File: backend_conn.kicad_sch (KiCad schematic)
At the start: 1 part, among them J2 QSH-030-01-X-D-A-XX

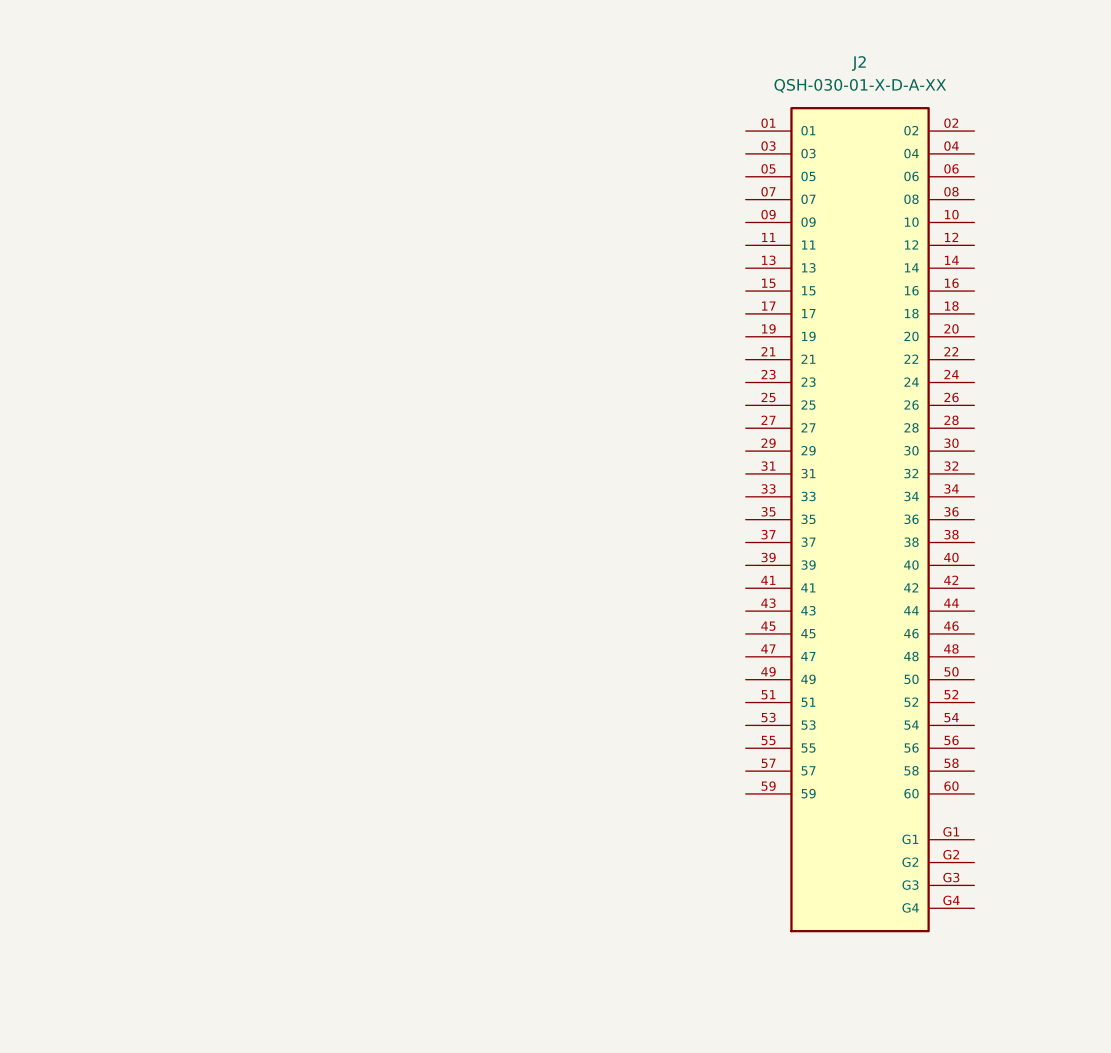
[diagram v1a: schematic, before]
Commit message: started changing package, added correct decoupling
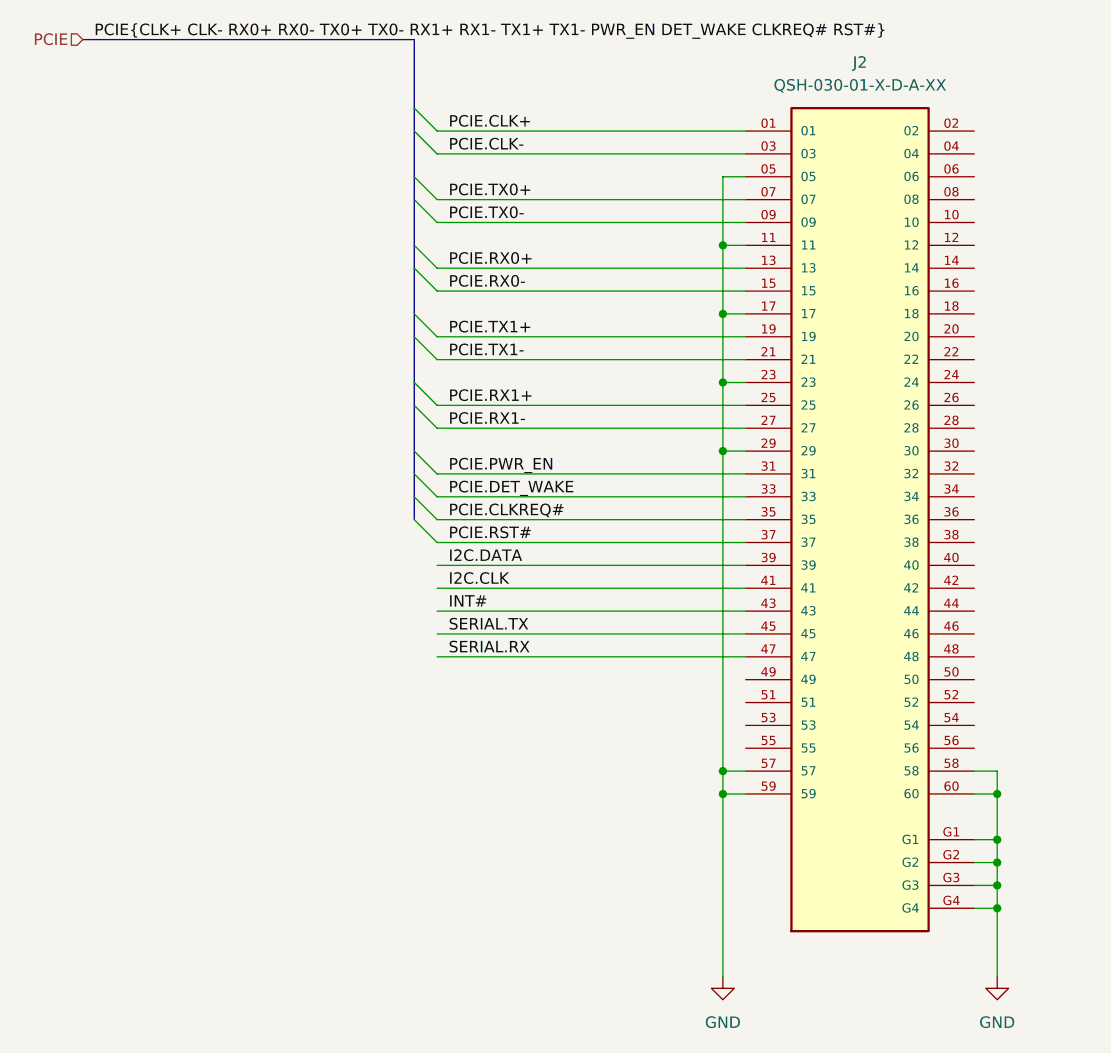
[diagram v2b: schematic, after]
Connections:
- net PCIE.CLK+: now reaches J2.01
- net PCIE.CLK-: now reaches J2.03
- net GND: now reaches J2.05
- net GND: now also J2.11, J2.17, J2.23, J2.29, J2.57, J2.58, J2.59, J2.60, J2.G1, J2.G2, J2.G3, J2.G4
- net PCIE.TX0+: now reaches J2.07
- net PCIE.TX0-: now reaches J2.09
- net PCIE.RX0+: now reaches J2.13
- net PCIE.RX0-: now reaches J2.15
- net PCIE.TX1+: now reaches J2.19
- net PCIE.TX1-: now reaches J2.21
- net PCIE.RX1+: now reaches J2.25
- net PCIE.RX1-: now reaches J2.27
- net PCIE.PWR_EN: now reaches J2.31
- net PCIE.DET_WAKE: now reaches J2.33
- net PCIE.CLKREQ#: now reaches J2.35
- net PCIE.RST#: now reaches J2.37
- net I2C.DATA: now reaches J2.39
- net I2C.CLK: now reaches J2.41
- net INT#: now reaches J2.43
- net SERIAL.TX: now reaches J2.45
- net SERIAL.RX: now reaches J2.47

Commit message: filled out back connector, finished ddr pinning according to vivado
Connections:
- net SPARE.LVDS0+: now reaches J2.02
- net SPARE.LVDS0-: now reaches J2.04
- net SPARE.LVDS1+: now reaches J2.06
- net SPARE.LVDS1-: now reaches J2.08
- net SPARE.LVDS2+: now reaches J2.10
- net SPARE.LVDS2-: now reaches J2.12
- net SPARE.LVDS3+: now reaches J2.14
- net SPARE.LVDS3-: now reaches J2.16
- net SPARE.LVDS4-: now reaches J2.18
- net SPARE.LVDS4+: now reaches J2.20
- net SPARE.LVDS5-: now reaches J2.22
- net SPARE.LVDS5+: now reaches J2.24
- net SPARE.LVDS6-: now reaches J2.26
- net SPARE.LVDS6+: now reaches J2.28
- net SPARE.LVDS7-: now reaches J2.30
- net SPARE.LVDS7+: now reaches J2.32
- net SPARE.LVDS8-: now reaches J2.34
- net SPARE.LVDS8+: now reaches J2.36
- net SPARE.LVDS9-: now reaches J2.38
- net SPARE.LVDS9+: now reaches J2.40
- net SPARE.LVDS10-: now reaches J2.42
- net SPARE.LVDS10+: now reaches J2.44
- net SPARE.LVDS11-: now reaches J2.46
- net SPARE.LVDS11+: now reaches J2.48
- net VBUS: now reaches J2.49
- net VBUS: now also J2.51, J2.53
- net SPARE.LVDS12-: now reaches J2.50
- net SPARE.LVDS12+: now reaches J2.52
- net +1V5: now reaches J2.54
- net +3.3V: now reaches J2.55
- net +1V8: now reaches J2.56

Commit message: started doing some general floorplanning and outline
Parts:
- added H5, H6, H7, H8: MountingHole_Pad, MountingHole:MountingHole_3.2mm_M3, symbol Mechanical:MountingHole_Pad
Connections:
- net GND: now also H5.1, H6.1, H7.1, H8.1

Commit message: more floorplanning
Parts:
- H5, H6, H7, H8: footprint MountingHole:MountingHole_3.2mm_M3 -> MountingHole:MountingHole_3.2mm_M3_DIN965_Pad
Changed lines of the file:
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@@
 			)
 		)
-		(property "Footprint" "MountingHole:MountingHole_3.2mm_M3"
+		(property "Footprint" "MountingHole:MountingHole_3.2mm_M3_DIN965_Pad"
 			(at 34.29 146.05 0)
 			(effects
@@
 			)
 		)
-		(property "Footprint" "MountingHole:MountingHole_3.2mm_M3"
+		(property "Footprint" "MountingHole:MountingHole_3.2mm_M3_DIN965_Pad"
 			(at 34.29 160.02 0)
 			(effects
@@
 			)
 		)
-		(property "Footprint" "MountingHole:MountingHole_3.2mm_M3"
+		(property "Footprint" "MountingHole:MountingHole_3.2mm_M3_DIN965_Pad"
 			(at 34.29 132.08 0)
 			(effects
@@
 			)
 		)
-		(property "Footprint" "MountingHole:MountingHole_3.2mm_M3"
+		(property "Footprint" "MountingHole:MountingHole_3.2mm_M3_DIN965_Pad"
 			(at 34.29 173.99 0)
 			(effects

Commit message: did alot of stuff
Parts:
- J2: LCSC (none) -> C5714556
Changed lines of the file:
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@@
+			)
+		)
+		(property "LCSC" "C5714556"
+			(at 152.4 93.98 0)
+			(effects
+				(font
+					(size 1.27 1.27)
+				)
 			)
 		)
